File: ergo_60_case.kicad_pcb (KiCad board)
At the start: 2 copper layers, 285 x 94.6 mm, 166 parts, among them SW1 SW_Push, U1 PRTR5V0U2X, U2 OLED_SSD1306, U3 AT90USB1286-AU, U4 AVR-ISP, Y1 16MHz

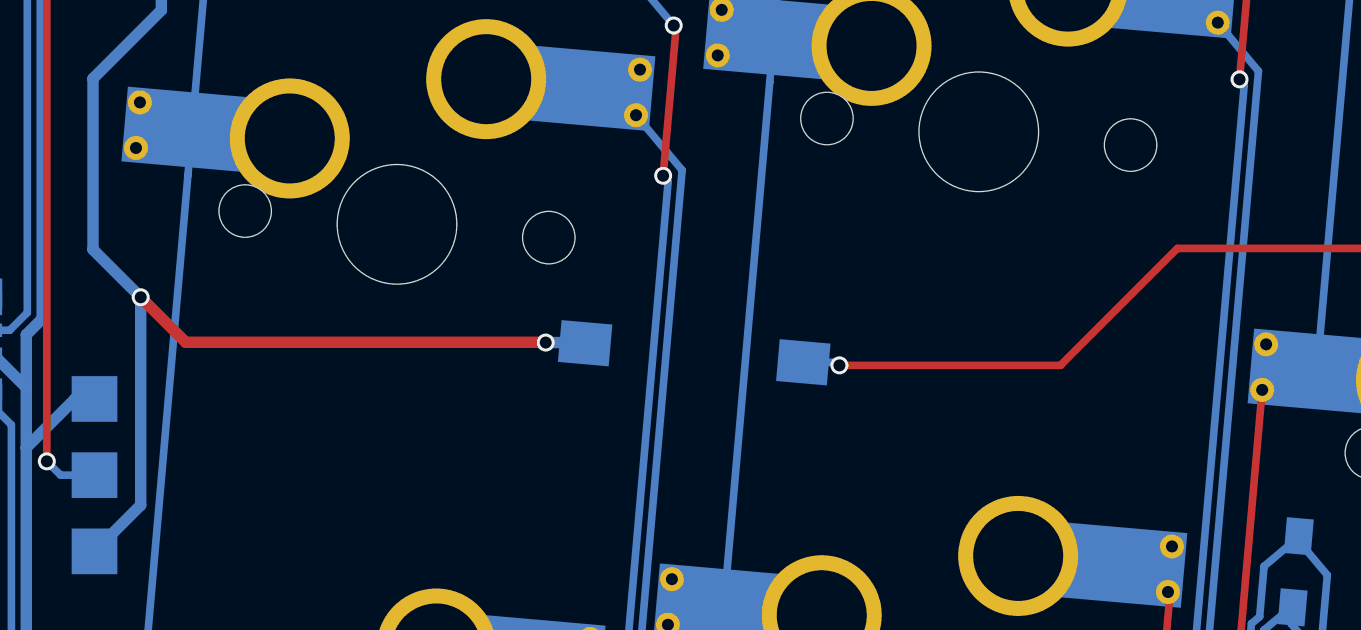
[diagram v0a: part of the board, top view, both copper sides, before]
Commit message: Revert "reset switch footprint correction"
This reverts commit f5c33ba12f206e91247782776fd24d7bcd64934f.
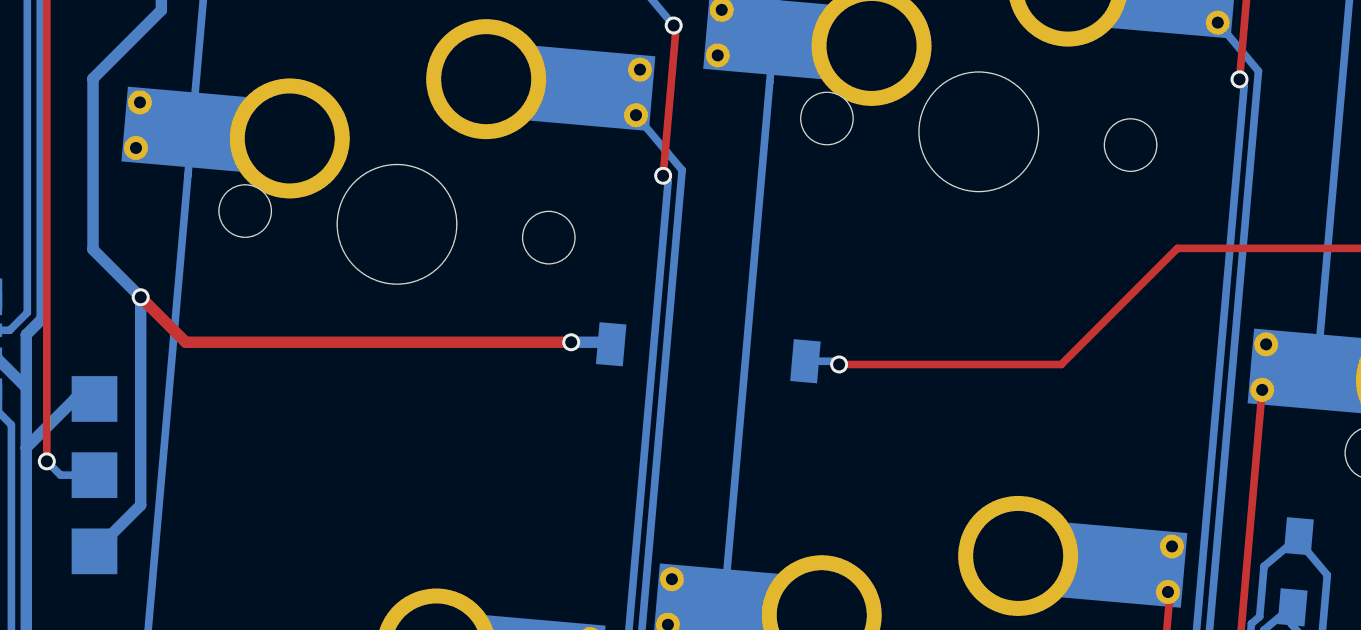
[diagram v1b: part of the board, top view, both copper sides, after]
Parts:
- moved SW1 0.47 mm to (93.2, 124.0)
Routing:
- net GND: track 1334.2 -> 1335.1 mm

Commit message: Revert "Revert "reset switch footprint correction""
This reverts commit 81e907175ec75a46385aedb48e9c2c01624081a1.
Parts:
- moved SW1 0.47 mm to (92.8, 124.0)
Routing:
- net GND: track 1335.1 -> 1334.2 mm
